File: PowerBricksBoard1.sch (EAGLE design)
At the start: 13 parts

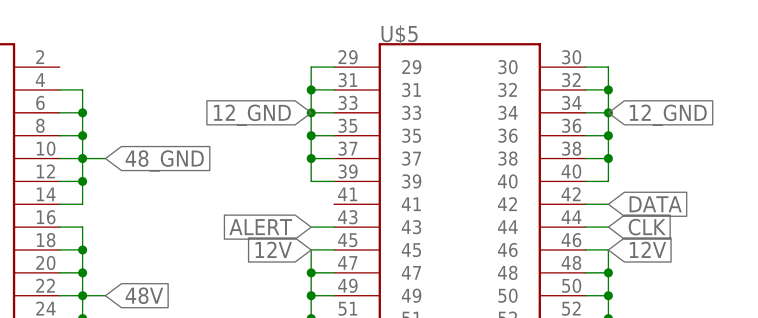
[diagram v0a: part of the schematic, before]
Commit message: cad for connectors
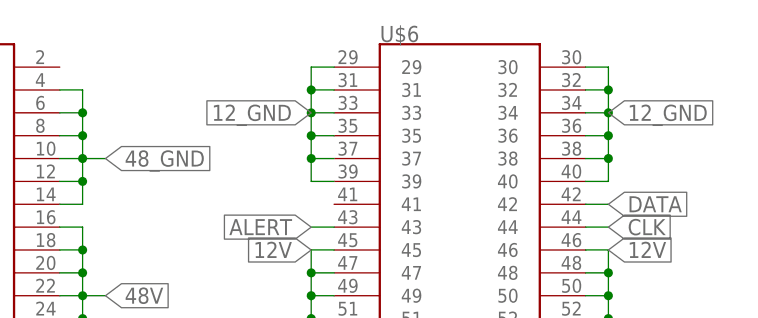
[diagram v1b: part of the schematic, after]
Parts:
- removed U$5: BRICKBOARD_TSW_14X2, Dist_to_Brickboard_Connector:BRICKBOARD_TSW_14X2
- added U$6: BRICKBOARD_TSW_14X2, Dist_to_Brickboard_Connector_brick:BRICKBOARD_TSW_14X2
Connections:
- net 12V: now also U$6.45, U$6.46, U$6.47, U$6.48, U$6.49, U$6.50, U$6.51, U$6.52, U$6.53, U$6.54, U$6.55, U$6.56; no longer U$5.45, U$5.46, U$5.47, U$5.48, U$5.49, U$5.50, U$5.51, U$5.52, U$5.53, U$5.54, U$5.55, U$5.56
- net 12_GND: now also U$6.29, U$6.30, U$6.31, U$6.32, U$6.33, U$6.34, U$6.35, U$6.36, U$6.37, U$6.38, U$6.39, U$6.40; no longer U$5.29, U$5.30, U$5.31, U$5.32, U$5.33, U$5.34, U$5.35, U$5.36, U$5.37, U$5.38, U$5.39, U$5.40
- net 48V: now also U$6.15, U$6.16, U$6.17, U$6.18, U$6.19, U$6.20, U$6.21, U$6.22, U$6.23, U$6.24, U$6.25, U$6.26, U$6.27, U$6.28; no longer U$5.15, U$5.16, U$5.17, U$5.18, U$5.19, U$5.20, U$5.21, U$5.22, U$5.23, U$5.24, U$5.25, U$5.26, U$5.27, U$5.28
- net 48_GND: now also U$6.10, U$6.11, U$6.12, U$6.13, U$6.14, U$6.3, U$6.4, U$6.5, U$6.6, U$6.7, U$6.8, U$6.9; no longer U$5.10, U$5.11, U$5.12, U$5.13, U$5.14, U$5.3, U$5.4, U$5.5, U$5.6, U$5.7, U$5.8, U$5.9
- net ALERT: now also U$6.43; no longer U$5.43
- net CLK: now also U$6.44; no longer U$5.44
- net DATA: now also U$6.42; no longer U$5.42
- net ON/OFF: now also U$6.1; no longer U$5.1

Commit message: Filled caps & ADDR resistors
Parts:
- added R3, R4: (no value), SparkFun-Resistors:RESISTOR0603
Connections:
- new net DGND: R3.1, R4.1, U$1.DGND
- new net N$3: R3.2, U$1.ADDR1
- new net N$4: R4.2, U$1.ADDR0
- net 48V: now also U$2.P$2, U$3.P$2, U$4.P$2; no longer U$2.P$1, U$3.P$1, U$4.P$1
- net 48_GND: now also U$2.P$1, U$3.P$1, U$4.P$1; no longer U$2.P$2, U$3.P$2, U$4.P$2
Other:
- moved on the sheet: U$2, U$3, U$4
